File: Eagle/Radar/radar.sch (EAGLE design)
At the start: 81 parts, among them IC4 MAX414ESD, X1 STEREOJACK, X2 BU-SMA-G, X3 BU-SMA-G, X4 BU-SMA-G

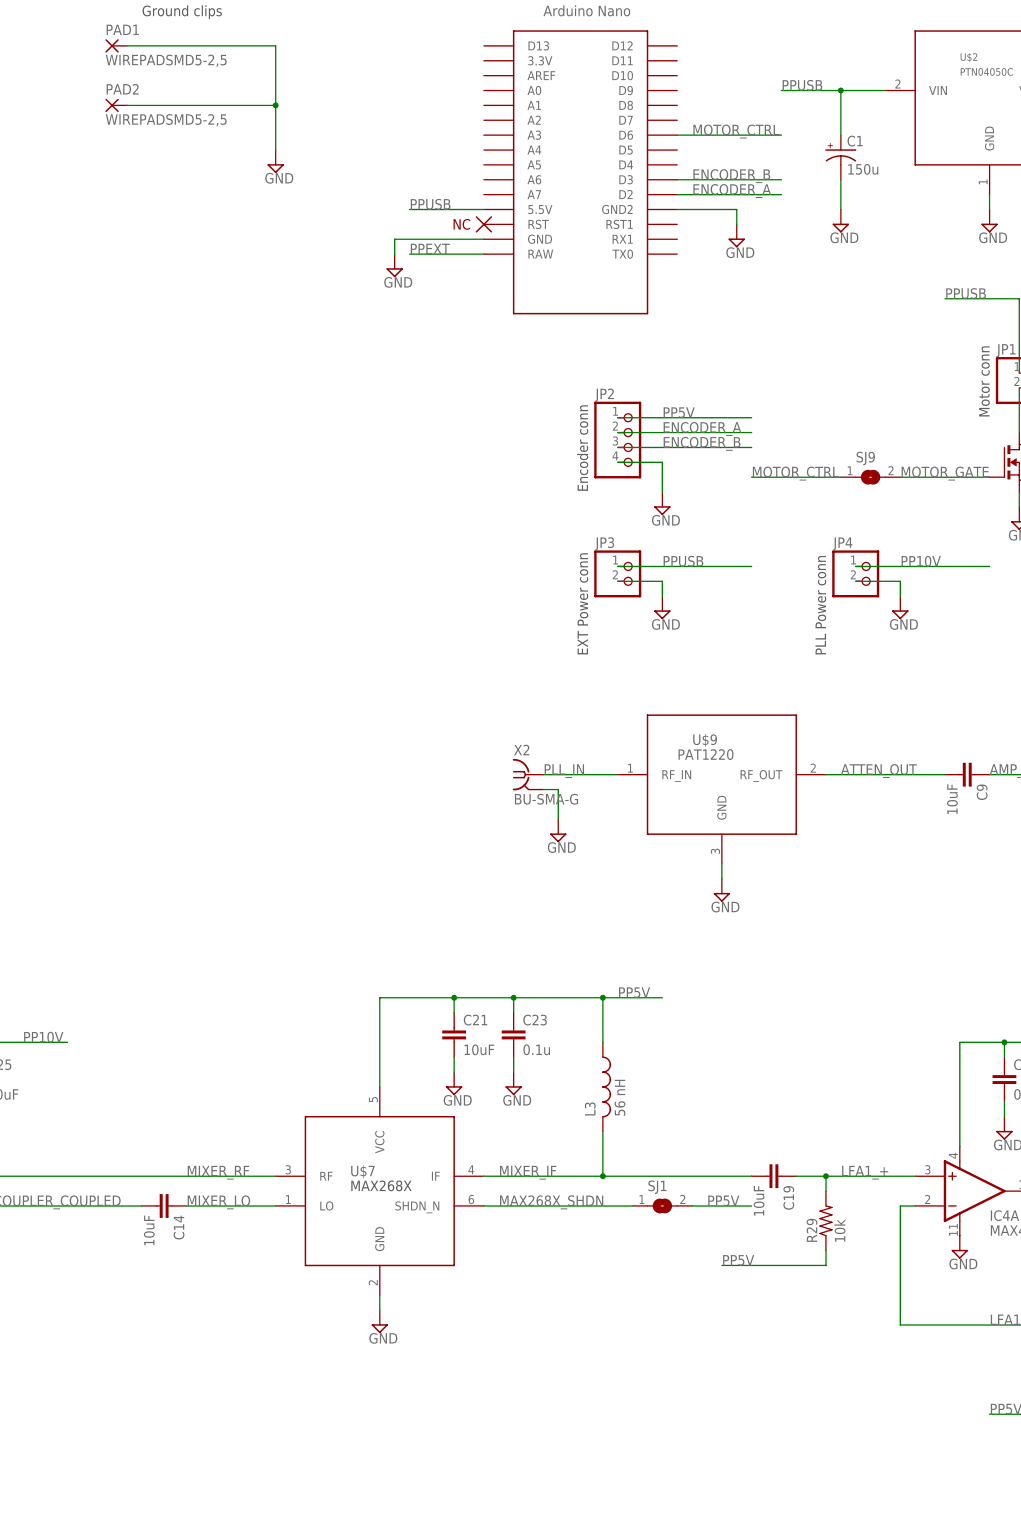
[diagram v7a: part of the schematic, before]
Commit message: Routes complete, no drc errors, no erc errors, need silks
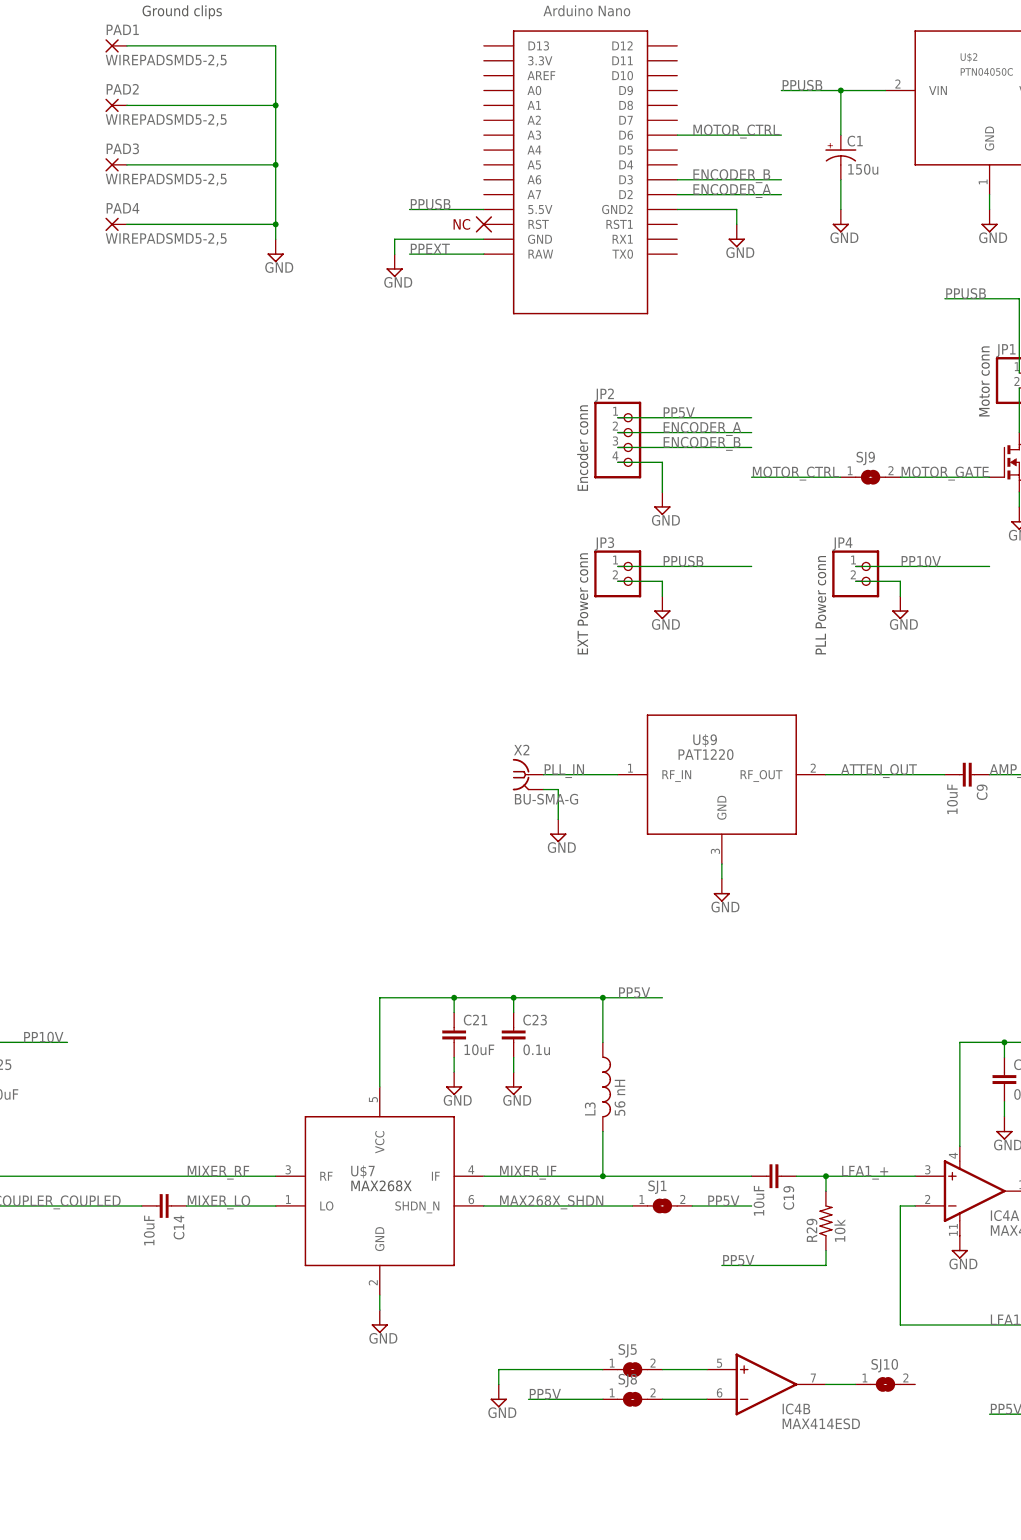
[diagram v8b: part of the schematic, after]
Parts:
- added PAD3, PAD4: WIREPADSMD5-2,5, wirepad:WIREPADSMD5-2,5
- added SJ10, SJ5, SJ8: (no value), jumper:SJ
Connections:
- new net N$2: IC4B.OUT, SJ10.1
- new net N$4: IC4B.+IN, SJ5.2
- new net N$5: IC4B.-IN, SJ8.2
- net GND: now also PAD3.P, PAD4.P, SJ5.1
- net PP5V: now also SJ8.1
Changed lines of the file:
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@@
 <part name="JP4" library="pinhead" deviceset="PINHD-1X2" device=""/>
 <part name="SUPPLY33" library="supply2" deviceset="GND" device=""/>
+<part name="PAD3" library="wirepad" deviceset="WIREPAD" device="SMD5-2,5"/>
+<part name="PAD4" library="wirepad" deviceset="WIREPAD" device="SMD5-2,5"/>
+<part name="SJ5" library="jumper" deviceset="SJ" device=""/>
+<part name="SJ8" library="jumper" deviceset="SJ" device=""/>
+<part name="SJ10" library="jumper" deviceset="SJ" device=""/>
+<part name="SUPPLY34" library="supply2" deviceset="GND" device=""/>
 </parts>
 <sheets>
@@
 <instance part="PAD1" gate="G$1" x="58.42" y="261.62"/>
 <instance part="PAD2" gate="G$1" x="58.42" y="251.46"/>
-<instance part="SUPPLY25" gate="GND" x="86.36" y="241.3"/>
+<instance part="SUPPLY25" gate="GND" x="86.36" y="226.06"/>
 <instance part="R18" gate="G$1" x="264.16" y="66.04">
 <attribute name="DIGI" x="264.16" y="66.04" size="1.778" layer="96" display="off"/>
@@
 <instance part="JP4" gate="G$1" x="187.96" y="170.18"/>
 <instance part="SUPPLY33" gate="GND" x="193.04" y="165.1"/>
+<instance part="PAD3" gate="G$1" x="58.42" y="241.3"/>
+<instance part="PAD4" gate="G$1" x="58.42" y="231.14"/>
+<instance part="IC4" gate="B" x="170.18" y="33.02"/>
+<instance part="SJ5" gate="1" x="147.32" y="35.56"/>
+<instance part="SJ8" gate="1" x="147.32" y="30.48"/>
+<instance part="SJ10" gate="1" x="190.5" y="33.02"/>
+<instance part="SUPPLY34" gate="GND" x="124.46" y="30.48"/>
 </instances>
 <busses>
@@
 <wire x1="86.36" y1="261.62" x2="86.36" y2="251.46" width="0.1524" layer="91"/>
 <pinref part="PAD2" gate="G$1" pin="P"/>
-<wire x1="86.36" y1="251.46" x2="86.36" y2="243.84" width="0.1524" layer="91"/>
+<wire x1="86.36" y1="251.46" x2="86.36" y2="241.3" width="0.1524" layer="91"/>
+<wire x1="86.36" y1="241.3" x2="86.36" y2="231.14" width="0.1524" layer="91"/>
+<wire x1="86.36" y1="231.14" x2="86.36" y2="228.6" width="0.1524" layer="91"/>
 <wire x1="60.96" y1="251.46" x2="86.36" y2="251.46" width="0.1524" layer="91"/>
 <junction x="86.36" y="251.46"/>
 <pinref part="SUPPLY25" gate="GND" pin="GND"/>
+<pinref part="PAD3" gate="G$1" pin="P"/>
+<wire x1="60.96" y1="241.3" x2="86.36" y2="241.3" width="0.1524" layer="91"/>
+<junction x="86.36" y="241.3"/>
+<pinref part="PAD4" gate="G$1" pin="P"/>
+<wire x1="60.96" y1="231.14" x2="86.36" y2="231.14" width="0.1524" layer="91"/>
+<junction x="86.36" y="231.14"/>
 </segment>
 <segment>
@@
 <pinref part="SUPPLY33" gate="GND" pin="GND"/>
 <wire x1="193.04" y1="167.64" x2="193.04" y2="170.18" width="0.1524" layer="91"/>
+</segment>
+<segment>
+<pinref part="SUPPLY34" gate="GND" pin="GND"/>
+<wire x1="124.46" y1="33.02" x2="124.46" y2="35.56" width="0.1524" layer="91"/>
+<pinref part="SJ5" gate="1" pin="1"/>
+<wire x1="124.46" y1="35.56" x2="142.24" y2="35.56" width="0.1524" layer="91"/>
 </segment>
 </net>
@@
 <pinref part="JP2" gate="A" pin="1"/>
 </segment>
+<segment>
+<pinref part="SJ8" gate="1" pin="1"/>
+<wire x1="142.24" y1="30.48" x2="129.54" y2="30.48" width="0.1524" layer="91"/>
+<label x="129.54" y="30.48" size="1.778" layer="95"/>
+</segment>
 </net>
 <net name="LDO1_FB" class="0">
@@
 </segment>
 </net>
+<net name="N$2" class="0">
+<segment>
+<pinref part="IC4" gate="B" pin="OUT"/>
+<pinref part="SJ10" gate="1" pin="1"/>
+<wire x1="180.34" y1="33.02" x2="185.42" y2="33.02" width="0.1524" layer="91"/>
+</segment>
+</net>
+<net name="N$4" class="0">
+<segment>
+<pinref part="SJ5" gate="1" pin="2"/>
+<pinref part="IC4" gate="B" pin="+IN"/>
+<wire x1="152.4" y1="35.56" x2="160.02" y2="35.56" width="0.1524" layer="91"/>
+</segment>
+</net>
+<net name="N$5" class="0">
+<segment>
+<pinref part="SJ8" gate="1" pin="2"/>
+<pinref part="IC4" gate="B" pin="-IN"/>
+<wire x1="152.4" y1="30.48" x2="160.02" y2="30.48" width="0.1524" layer="91"/>
+</segment>
+</net>
 </nets>
 </sheet>
 </sheets>
+<errors>
+</errors>
 </schematic>
 </drawing>
